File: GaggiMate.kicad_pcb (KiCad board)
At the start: 4 copper layers, 76 x 90.1 mm, 61 parts, among them J1 BTNS, J10 K-Type probe, J11 HV In, J12 Relays, J13 Analog sensors, J14 Pressure Sensor, J2 Heater SSR, J3 K-Type probe, J5 Analog sensors, J6 Pressure Sensor, J8 HV In, J9 Relays, P0 USB_C_Plug_USB2.0, SW1 SW_Push, SW2 SW_Push, U0 ADS1115IDGS, U1 MAX31855KASA, U2 ESP32-S3-WROOM-1, U3 AQH2223A, U4 USBLC6-2SC6, U5 AQH2223A, U6 AMS1117-3.3

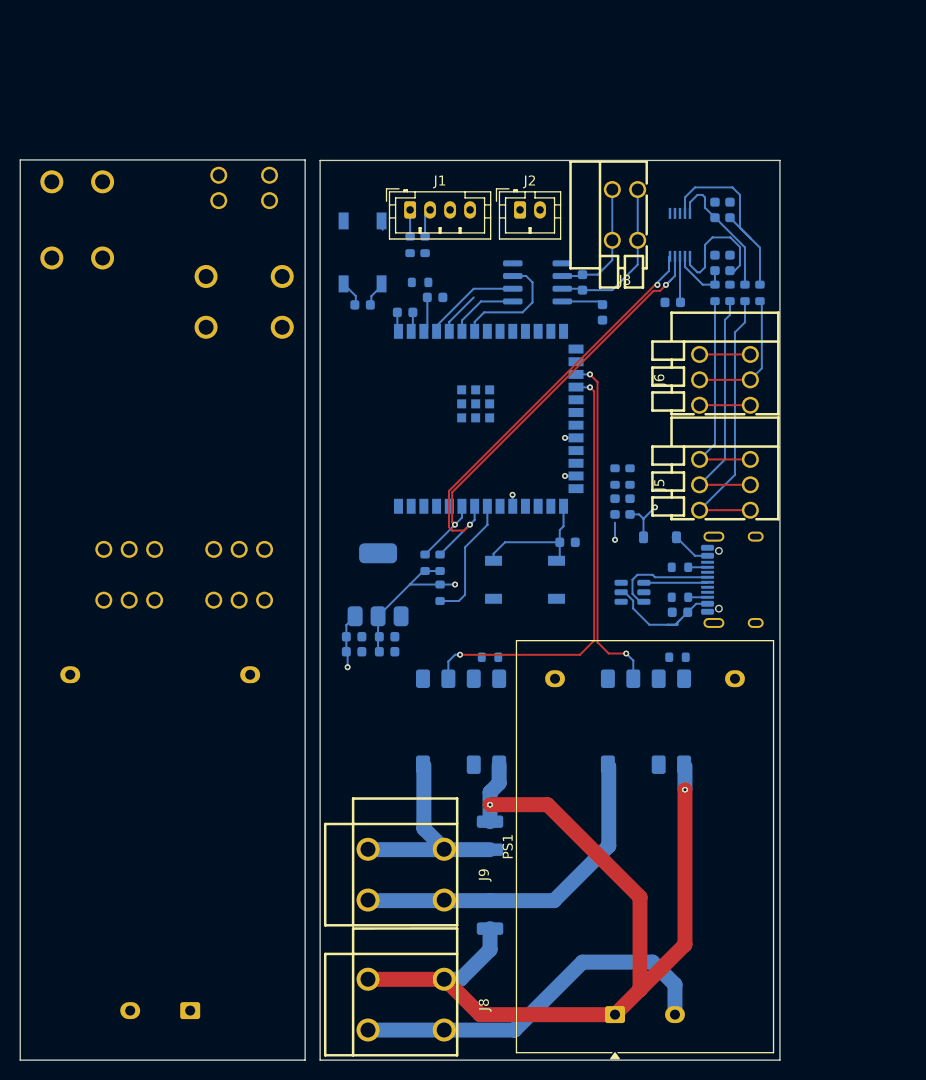
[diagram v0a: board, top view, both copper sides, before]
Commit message: update layout a lot
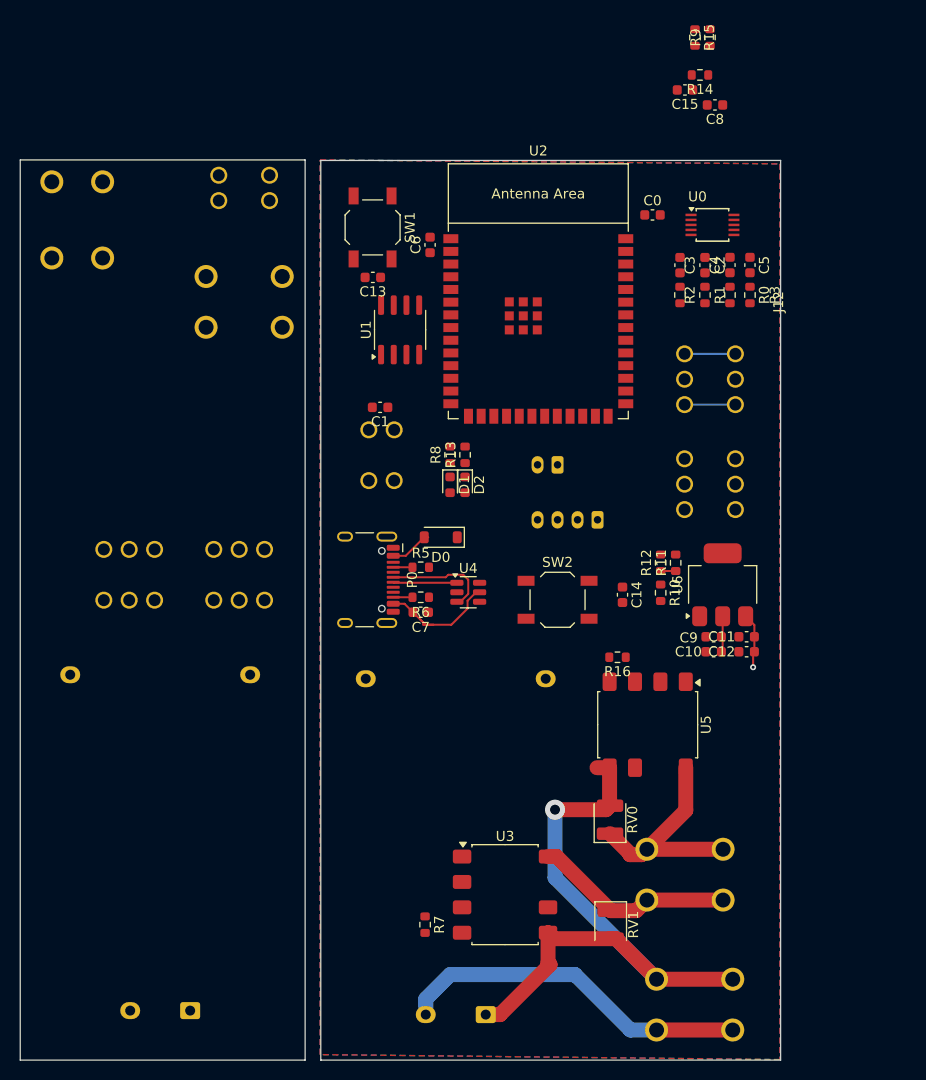
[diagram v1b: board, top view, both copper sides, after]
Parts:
- C0, C1, C10, C11, C12, C13, C14, C15, C2, C3, C4, C5, C6, C7, C8, C9, D0, D1, D2, P0, R0, R1, R10, R11, R12, R13, R14, R15, R16, R2, R3, R5, R6, R7, R8, R9, RV0, RV1, SW1, SW2, U0, U1, U2, U3, U4, U5, U6: moved to F.Cu
- J1, J2, J3, J5, J6, J8, J9, PS1: moved to B.Cu
- moved C11 39.3 mm to (152.7, 97.7), turned to 0 degrees
- moved C12 39.3 mm to (152.7, 99.2), turned to 180 degrees
- moved P0 38.9 mm to (113.6, 92.0)
- moved C8 37.3 mm to (149.5, 44.5), turned to 180 degrees
- moved R7 36.8 mm to (120.5, 126.5), turned to -90 degrees
- moved R9 36.5 mm to (149.0, 37.8)
- moved J1 36.2 mm to (137.8, 86.0), turned to 180 degrees
- moved R14 34.9 mm to (148.0, 41.5), turned to 180 degrees
- moved U6 34.5 mm to (150.3, 92.5)
- moved J3 34.2 mm to (116.1, 79.5)
- moved R15 34.1 mm to (147.5, 37.8)
- moved C10 32.7 mm to (149.4, 99.2), turned to 180 degrees
- moved C9 32.7 mm to (149.4, 97.7), turned to 180 degrees
- moved C15 32.5 mm to (146.5, 43.0), turned to 180 degrees
- moved J8 28.9 mm to (147.5, 134.5)
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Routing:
- net I2C_SCL: track 45.1 -> 0.00 mm, vias 2 -> 0
- net VALVE: track 44.1 -> 0.00 mm, vias 2 -> 0
- net I2C_SDA: track 43.7 -> 0.00 mm, vias 2 -> 0
- net 3.3V: track 48.6 -> 5.10 mm, vias 2 -> 0
- net PUMP: track 34.7 -> 0.00 mm, vias 2 -> 0
- net HV_L: track 96.0 -> 64.1 mm, vias 2 -> 1
- net AIN1: track 27.9 -> 0.00 mm
- net AIN2: track 24.7 -> 0.00 mm
- net AIN3: track 21.6 -> 0.00 mm
- net Net-(U0-AIN0): track 20.6 -> 0.00 mm
- net T+: track 16.2 -> 0.00 mm
- net HV_PUMP: track 34.2 -> 20.2 mm
- net BOOT: track 13.5 -> 0.00 mm
- net PRESSURE: track 13.5 -> 0.00 mm
- net Net-(U0-AIN1): track 13.4 -> 0.00 mm
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- added copper zone on In2.Cu, net 5V
- added copper zone on B.Cu, net GND
- added copper zone on F.Cu, net GND
- added copper zone on In1.Cu, net GND
- added copper zone on In2.Cu, net GND
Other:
- board size 76 x 90.1 mm -> 76.1 x 90.1 mm

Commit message: finalize layout and tracks?
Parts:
- moved R15 61.2 mm to (138.2, 98.2), turned to 0 degrees
- moved R9 60.0 mm to (138.2, 96.8), turned to 180 degrees
- moved C15 38.4 mm to (113.5, 62.7)
- moved R11 38.3 mm to (146.0, 52.0), turned to 180 degrees
- moved R10 35.6 mm to (144.5, 57.8), turned to 180 degrees
- moved R12 35.1 mm to (144.2, 55.2), turned to 180 degrees
- moved R14 31.9 mm to (118.5, 53.7), turned to -90 degrees
- moved C8 31.4 mm to (121.3, 58.4), turned to -90 degrees
- moved C14 14.5 mm to (140.0, 79.0), turned to 180 degrees
- moved C6 14.0 mm to (120.0, 72.5), turned to -90 degrees
- moved R16 12.5 mm to (152.0, 102.0)
- moved SW2 12.0 mm to (140.8, 84.2), turned to -90 degrees
- moved R7 11.9 mm to (117.5, 115.0)
- moved C13 9.31 mm to (114.8, 52.5)
- moved U3 6.80 mm to (122.0, 121.5)
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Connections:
- net Net-(P0-D+) renamed /D+
- net Net-(P0-D-) renamed /D-
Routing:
- net 5V: track 82.8 -> 10.5 mm, vias 1 -> 2
- net PUMP: track 0.00 -> 52.6 mm
- net VALVE: track 0.00 -> 33.9 mm
- net BREW_BTN: track 0.00 -> 31.5 mm, vias 0 -> 1
- net STEAM_BTN: track 0.00 -> 24.7 mm, vias 0 -> 1
- net AIN1: track 0.00 -> 23.7 mm
- net AIN2: track 0.00 -> 23.6 mm
- net 3.3V: track 5.10 -> 26.2 mm, vias 0 -> 9
- net EN: track 0.00 -> 20.3 mm
- net AIN3: track 0.00 -> 20.1 mm
- net USB_D-: track 0.00 -> 19.8 mm
- net I2C_SDA: track 0.00 -> 18.9 mm
- net USB_D+: track 0.00 -> 17.8 mm
- net I2C_SCL: track 0.00 -> 16.9 mm
- net RDY: track 0.00 -> 16.1 mm
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- added copper zone on In2.Cu, net 3.3V

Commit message: some updates
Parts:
- added J4: Conn_02x08_Odd_Even, Connector_PinHeader_2.54mm:PinHeader_2x08_P2.54mm_Vertical_SMD, B.Cu at (164.5, 45.9)
- added J7: Debug Pins, Connector_PinHeader_2.54mm:PinHeader_2x05_P2.54mm_Vertical_SMD, B.Cu at (132.0, 72.5)
- moved C7 2.01 mm to (120.2, 97.2), turned to -90 degrees
- moved R6 1.40 mm to (121.2, 94.5)
- moved R11 1.25 mm to (144.8, 52.0), turned to 0 degrees
- moved C1 0.25 mm to (116.2, 74.0)
- turned C4 to 90 degrees
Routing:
- net VALVE: track 33.9 -> 42.0 mm
- net USB_D+: track 17.8 -> 25.6 mm
- net USB_D-: track 19.8 -> 25.6 mm
- net GND: track 17.8 -> 12.7 mm, vias 33 -> 34
- net T+: track 15.4 -> 13.5 mm
- net Net-(P0-VCONN): track 1.93 -> 3.42 mm
- net Net-(U0-AIN2): track 12.8 -> 14.3 mm
- net 5V: track 10.5 -> 11.2 mm
- net 3.3V: track 26.2 -> 25.7 mm, vias 9 -> 10

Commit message: release candidate 1
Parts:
- removed C7: 10uF, Capacitor_SMD:C_0603_1608Metric
- removed D0: 1N5817, Diode_SMD:D_SOD-123
- removed J12: Relays, easyeda2kicad:CONN-TH_2P-P5.08_DIBO_DB142V-5.08-2P
- removed J13: Analog sensors, easyeda2kicad:CONN-TH_3P-P2.54_DIBO_DB141V-2.54-3P
- removed J14: Pressure Sensor, easyeda2kicad:CONN-TH_3P-P2.54_DIBO_DB141V-2.54-3P
- removed J7: Debug Pins, Connector_PinHeader_2.54mm:PinHeader_2x05_P2.54mm_Vertical_SMD
- removed P0: USB_C_Plug_USB2.0, Connector_USB:USB_C_Receptacle_HCTL_HC-TYPE-C-16P-01A
- removed PS2: HLK-5M05, Converter_ACDC:Converter_ACDC_Hi-Link_HLK-5Mxx
- removed the R5 at (120.1, 90.8)
- removed R6: 5.1k, Resistor_SMD:R_0603_1608Metric
- removed U3, U5: AQH2223A, Package_SO:SSO-7-8_6.4x9.78mm_P2.54mm
- added C16: 10uF, Capacitor_SMD:C_0603_1608Metric, F.Cu at (119.8, 96.2)
- added D3: 1N5817, Diode_SMD:D_SOD-123, F.Cu at (114.0, 98.5)
- added R17: 5.1k, Resistor_SMD:R_0603_1608Metric, F.Cu at (120.8, 87.2)
- added R4: 5.1k, Resistor_SMD:R_0603_1608Metric, F.Cu at (122.5, 94.8)
- added TP1: TestPoint, TestPoint:TestPoint_Pad_D1.0mm, F.Cu at (117.6, 101.6)
- added TP10: TestPoint, TestPoint:TestPoint_Pad_D1.0mm, F.Cu at (124.5, 82.8)
- added TP2: TestPoint, TestPoint:TestPoint_Pad_D1.0mm, F.Cu at (119.0, 99.7)
- added TP3: TestPoint, TestPoint:TestPoint_Pad_D1.0mm, F.Cu at (122.5, 80.2)
- added TP4: TestPoint, TestPoint:TestPoint_Pad_D1.0mm, F.Cu at (145.4, 61.6)
- added TP5: TestPoint, TestPoint:TestPoint_Pad_D1.0mm, F.Cu at (148.0, 61.6)
- added TP6: TestPoint, TestPoint:TestPoint_Pad_D1.0mm, B.Cu at (122.0, 61.5)
- added TP7: TestPoint, TestPoint:TestPoint_Pad_D1.0mm, B.Cu at (120.5, 63.0)
- added TP8: TestPoint, TestPoint:TestPoint_Pad_D1.0mm, B.Cu at (119.0, 64.5)
- added TP9: TestPoint, TestPoint:TestPoint_Pad_D1.0mm, F.Cu at (112.4, 63.3)
- added U7: GT-USB-7010ASV, easyeda2kicad:USB-C-SMD_G-SWITCH_GT-USB-7010ASV, F.Cu at (115.3, 91.0)
- added U8: USBLC6-2SC6, Package_TO_SOT_SMD:SOT-23-6, F.Cu at (121.9, 91.0)
- added U9: AQH2223A, easyeda2kicad:SMD-8_7P-L9.8-W6.4-P2.54-BL-PE7, F.Cu at (120.5, 122.5)
- J10: value K-Type probe -> UART; footprint easyeda2kicad:CONN-TH_2P-P2.54_DIBO_DB141V-2.54-2P -> Connector_PinHeader_2.54mm:PinHeader_2x02_P2.54mm_Vertical_SMD
- J11: value HV In -> Fun breakout; footprint easyeda2kicad:CONN-TH_2P-P5.08_DIBO_DB142V-5.08-2P -> Connector_PinHeader_2.54mm:PinHeader_2x03_P2.54mm_Vertical_SMD
- J4: value Conn_02x08_Odd_Even -> HX771; footprint Connector_PinHeader_2.54mm:PinHeader_2x08_P2.54mm_Vertical_SMD -> Connector_PinHeader_2.54mm:PinHeader_2x02_P2.54mm_Vertical_SMD
- RV0, RV1: footprint Diode_SMD:D_1210_3225Metric -> easyeda2kicad:RES-SMD_L6.8-W5.9-LS7.8
- U4: value USBLC6-2SC6 -> AQH2223A; footprint Package_TO_SOT_SMD:SOT-23-6 -> easyeda2kicad:SMD-8_7P-L9.8-W6.4-P2.54-BL-PE7
- moved J11 48.7 mm to (127.0, 81.8)
- moved C12 39.9 mm to (113.2, 105.2), turned to -90 degrees
- moved C11 38.6 mm to (114.8, 105.2), turned to 90 degrees
- moved J4 37.1 mm to (136.7, 70.4), turned to -90 degrees
- moved C13 34.9 mm to (133.0, 82.2)
- moved SW1 34.9 mm to (133.0, 87.2)
- moved U6 33.0 mm to (120.8, 107.5), turned to -90 degrees
- moved J10 30.3 mm to (131.8, 60.2), turned to 0 degrees
- moved R8 29.9 mm to (116.2, 108.2), turned to -90 degrees
- moved C9 27.5 mm to (122.1, 101.4), turned to 0 degrees
- moved C10 27.3 mm to (122.1, 99.9), turned to 0 degrees
- moved D1 24.0 mm to (116.2, 105.2), turned to 90 degrees
- moved U4 19.8 mm to (139.0, 106.2), turned to 180 degrees
- moved C2 14.9 mm to (144.5, 77.5), turned to 180 degrees
- moved R1 14.1 mm to (145.2, 79.8)
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- renumbered R7 to R16, R16 to R5
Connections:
- D2 pad 2: 3.3V -> EN
- J10 pad 1: unconnected-(J10-Pin_1-Pad1) -> U0CTS
- J10 pad 2: unconnected-(J10-Pin_2-Pad2)_1 -> U0RXD
- J11 pad 1: unconnected-(J11-Pin_1-Pad1)_1 -> IO1
- J11 pad 2: unconnected-(J11-Pin_2-Pad2)_1 -> GND
- J4 pad 1: /A0 -> I2C_SDA
- J4 pad 2: /A6 -> GND
- J4 pad 3: /A1 -> I2C_SCL
- J4 pad 4: /A7 -> 3.3V
- R16 pad 1: GND -> PUMP
- R5 pad 1: GND -> VALVE
- R5 pad 2: Net-(R16-Pad2) (its old number) -> Net-(R5-Pad2)
- U2 pad 10: /A9 -> IO5
- U2 pad 11: /A10 -> IO6
- U2 pad 12: /A5 -> IO1
- U2 pad 15: /A4 -> Net-(U2-GPIO3/TOUCH3/ADC1_CH2)
- U2 pad 16: /A13 -> Net-(U2-GPIO46)
- U2 pad 19: /A6 -> IO2
- U2 pad 20: /A7 -> IO3
- U2 pad 21: /A8 -> unconnected-(U2-GPIO13/TOUCH13/ADC2_CH2/FSPIQ/FSPIIO7/SUBSPIQ-Pad21)
- U2 pad 23: /A11 -> unconnected-(U2-GPIO21-Pad23)
- U2 pad 26: /A12 -> unconnected-(U2-GPIO45-Pad26)
- U2 pad 38: /A3 -> unconnected-(U2-GPIO2/TOUCH2/ADC1_CH1-Pad38)
- U2 pad 39: /A2 -> unconnected-(U2-GPIO1/TOUCH1/ADC1_CH0-Pad39)
- U4 pad 1: /D- -> GND
- U4 pad 2: GND -> Net-(R5-Pad2)
- U4 pad 3: /D+ -> GND
- U4 pad 4: USB_D+ -> GND
- U4 pad 5: Net-(D0-A) -> unconnected-(U4-Pad5)
- U4 pad 6: USB_D- -> HV_L
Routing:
- net 5V: track 11.2 -> 62.8 mm, vias 2 -> 0
- net EN: track 20.3 -> 57.6 mm, vias 0 -> 2
- net Net-(D3-A): track 0.00 -> 27.5 mm, vias 0 -> 4
- net Net-(D0-A): track 25.7 -> 0.00 mm
- net IO6: track 0.00 -> 18.2 mm, vias 0 -> 1
- net IO5: track 0.00 -> 16.7 mm, vias 0 -> 1
- net GND: track 12.7 -> 26.9 mm, vias 34 -> 75
- net IO3: track 0.00 -> 13.9 mm, vias 0 -> 1
- net HEATER: track 11.6 -> 24.7 mm
- net U0RTS: track 0.00 -> 12.2 mm, vias 0 -> 1
- net PUMP: track 52.6 -> 40.8 mm
- net IO2: track 0.00 -> 11.1 mm, vias 0 -> 1
- net IO1: track 0.00 -> 10.8 mm, vias 0 -> 1
- net U0CTS: track 0.00 -> 10.8 mm, vias 0 -> 1
- net 3.3V: track 25.7 -> 35.1 mm
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- removed copper zone on In2.Cu, net 5V
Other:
- board size 76.1 x 90.1 mm -> 46 x 90 mm

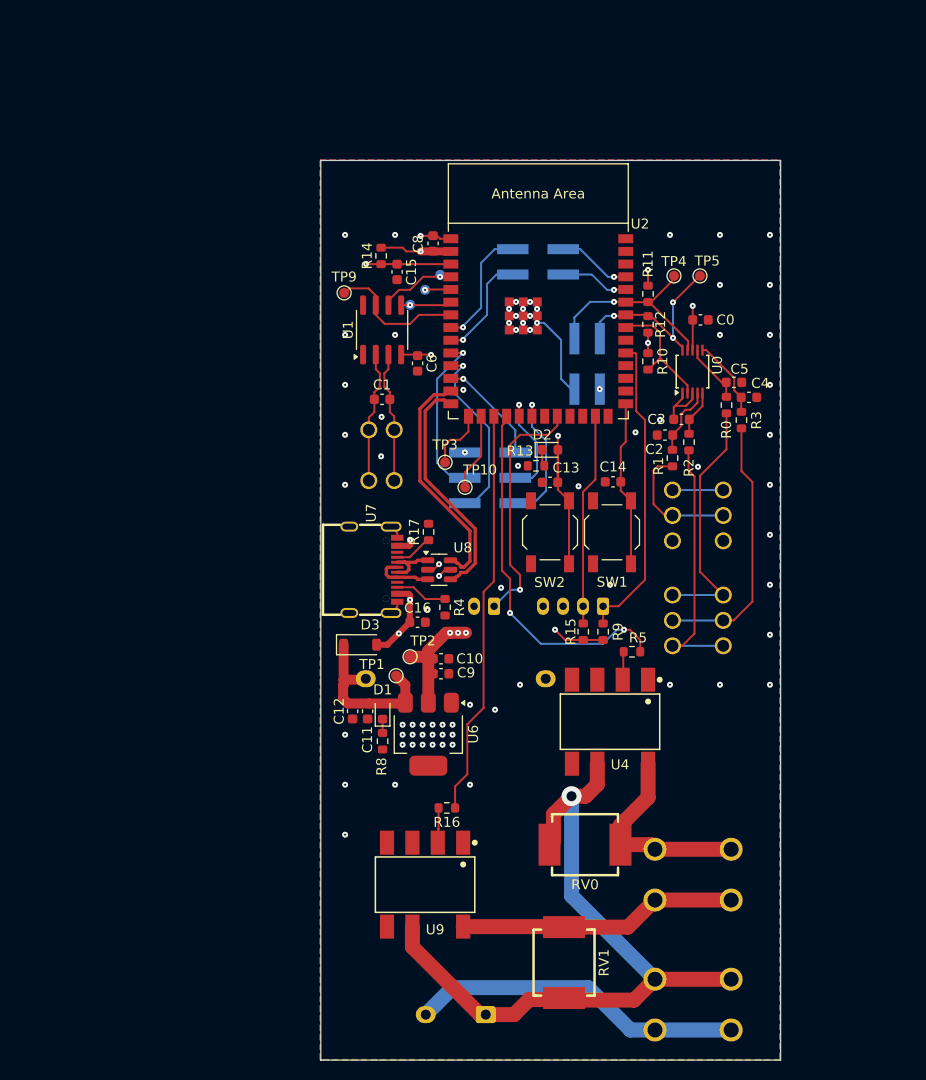
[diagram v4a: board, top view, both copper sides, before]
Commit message: add custom silkscreen and missing lilygo out pins
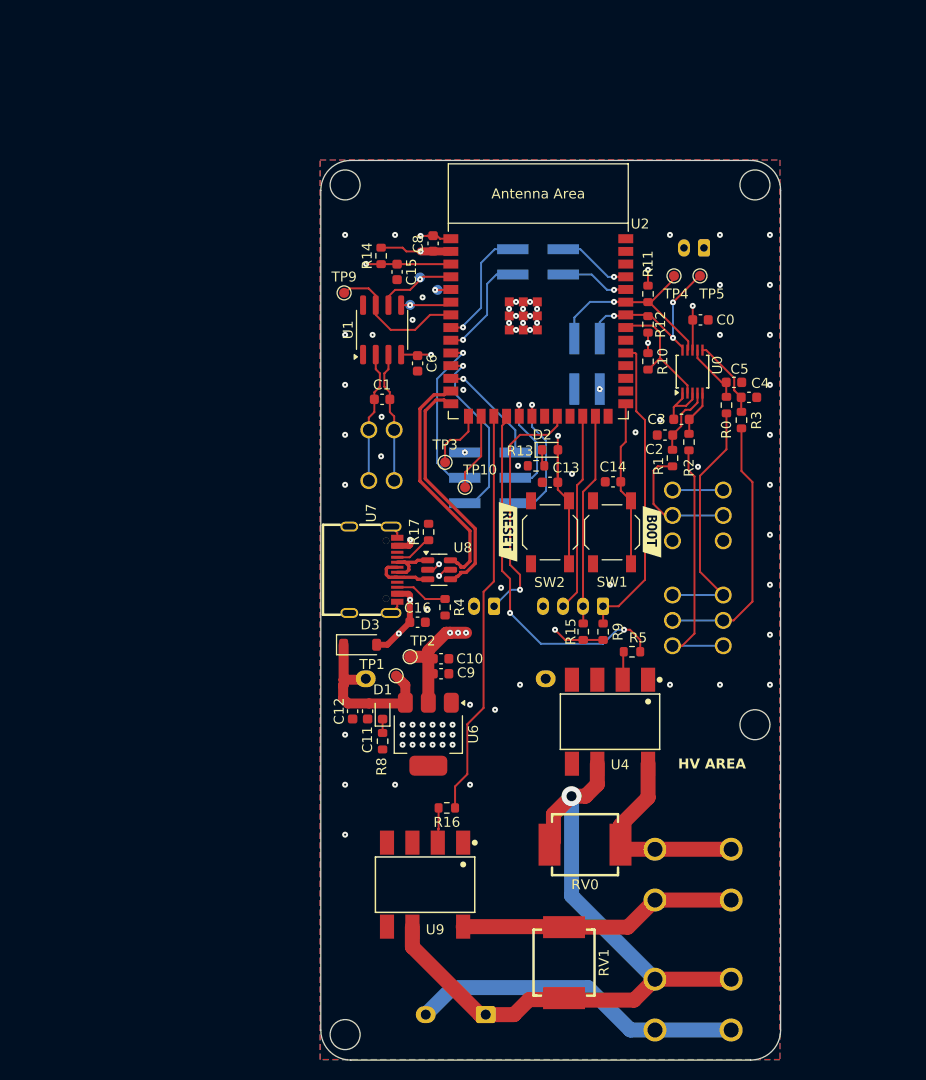
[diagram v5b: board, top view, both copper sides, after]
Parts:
- added G***: LOGO, Custom:gaggia_silkscreen, B.Cu at (148.0, 70.4)
- added J7: LILYGO, Connector_JST:JST_PH_B2B-PH-K_1x02_P2.00mm_Vertical, B.Cu at (148.4, 58.8)
- added kibuzzard-68D853DB: G***, kibuzzard-68D853DB, B.Cu at (131.8, 90.6)
- added kibuzzard-68D853DB: G***, kibuzzard-68D853DB, B.Cu at (125.4, 90.8)
- added kibuzzard-68D85755: G***, kibuzzard-68D85755, B.Cu at (141.8, 59.2)
- added kibuzzard-68D85864: G***, kibuzzard-68D85864, B.Cu at (140.4, 82.5)
- added kibuzzard-68D85872: G***, kibuzzard-68D85872, B.Cu at (138.8, 84.5)
- added kibuzzard-68D85884: G***, kibuzzard-68D85884, B.Cu at (140.2, 86.5)
- added kibuzzard-68D8588D: G***, kibuzzard-68D8588D, B.Cu at (133.8, 90.4)
- added kibuzzard-68D85899: G***, kibuzzard-68D85899, B.Cu at (135.8, 89.6)
- added kibuzzard-68D8589E: G***, kibuzzard-68D8589E, B.Cu at (137.8, 90.0)
- added kibuzzard-68D858A7: G***, kibuzzard-68D858A7, B.Cu at (127.4, 89.6)
- added kibuzzard-68D858C6: G***, kibuzzard-68D858C6, B.Cu at (153.2, 59.2)
- added kibuzzard-68D85940: G***, kibuzzard-68D85940, B.Cu at (139.8, 132.0)
- added kibuzzard-68D85954: G***, kibuzzard-68D85954, B.Cu at (139.8, 137.0)
- added kibuzzard-68D8595E: G***, kibuzzard-68D8595E, B.Cu at (139.4, 122.6)
- added kibuzzard-68D859D6: G***, kibuzzard-68D859D6, B.Cu at (139.4, 117.4)
- added kibuzzard-68D85A63: G***, kibuzzard-68D85A63, F.Cu at (143.2, 87.2)
- added kibuzzard-68D85A7C: G***, kibuzzard-68D85A7C, F.Cu at (128.8, 87.2)
- added kibuzzard-68D85AF0: G***, kibuzzard-68D85AF0, B.Cu at (117.4, 69.8)
- added kibuzzard-68D85B00: G***, kibuzzard-68D85B00, B.Cu at (114.8, 69.8)
- moved TP6 2.02 mm to (120.0, 61.8)
- moved TP7 1.25 mm to (121.8, 63.0)
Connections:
- J1 pad 3: GND -> ALT
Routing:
- net ALT: track 0.00 -> 19.8 mm
- net GND: track 26.9 -> 18.2 mm, vias 75 -> 77
- net SPI_MOSI: track 2.59 -> 1.59 mm
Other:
- outline, holes or cut-outs redrawn
- board text added: "3V3 SCL GND SDA"
- board text added: "A3 A2 A1"
- board text added: "By blennster"
- board text added: "GaggiBro V1"
- board text added: "HV AREA"
- board text added: "IO3 IO2 IO1 IO6 IO5 GND"
- board text added: "MISO MOSI CLK"
- board text added: "TX RTS RX CTS"
